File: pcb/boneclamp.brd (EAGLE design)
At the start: 160 x 100 mm, 39 parts, among them U1 AD7656YSTZ, U2 AD5754RBREZ, U3 SN74ABT541BDW, U4 ADP3303ARZ-5, U5 ADP3303ARZ-5

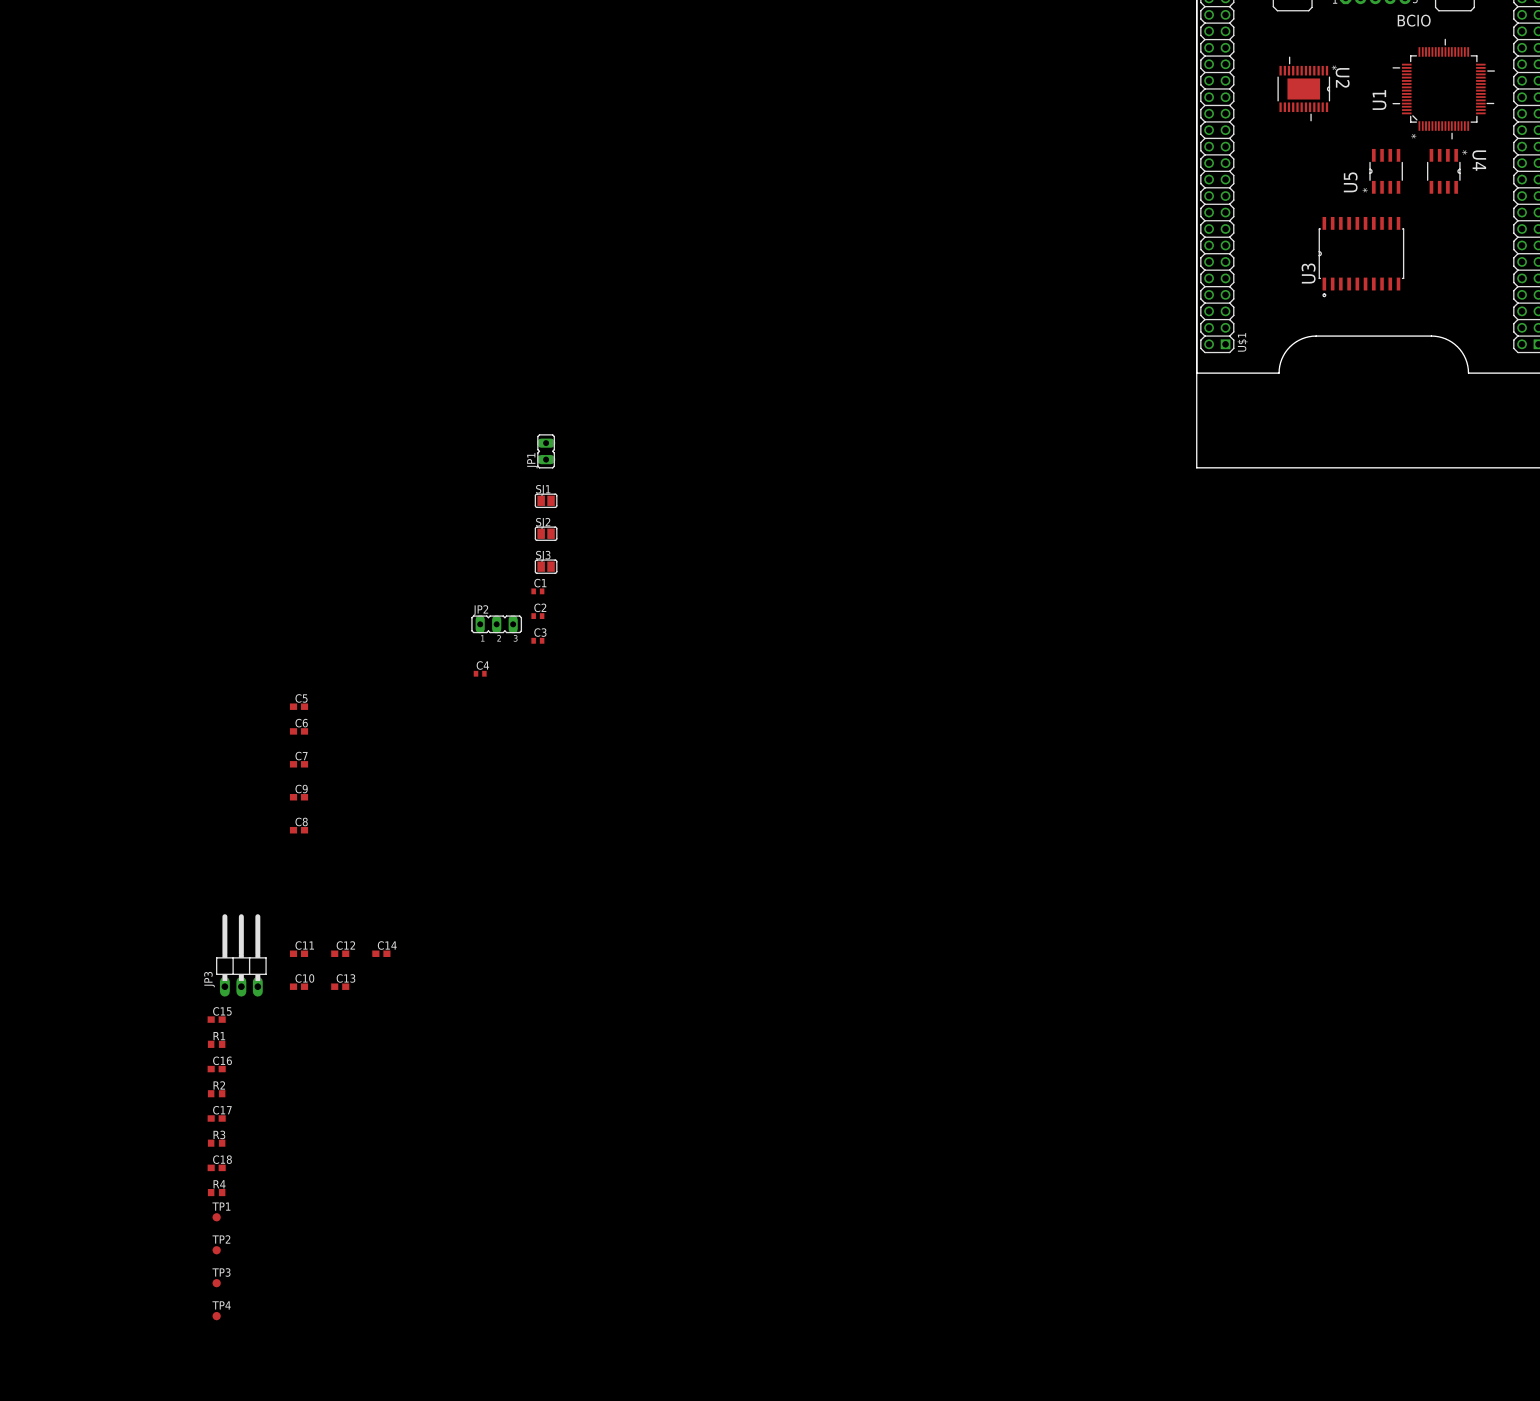
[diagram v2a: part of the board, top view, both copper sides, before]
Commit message: Found a good regulator for powering the BB using the +/- 6 to 12 volt rails required to use the boneclamp. Updated schematic and added data sheet to data-sheets folder
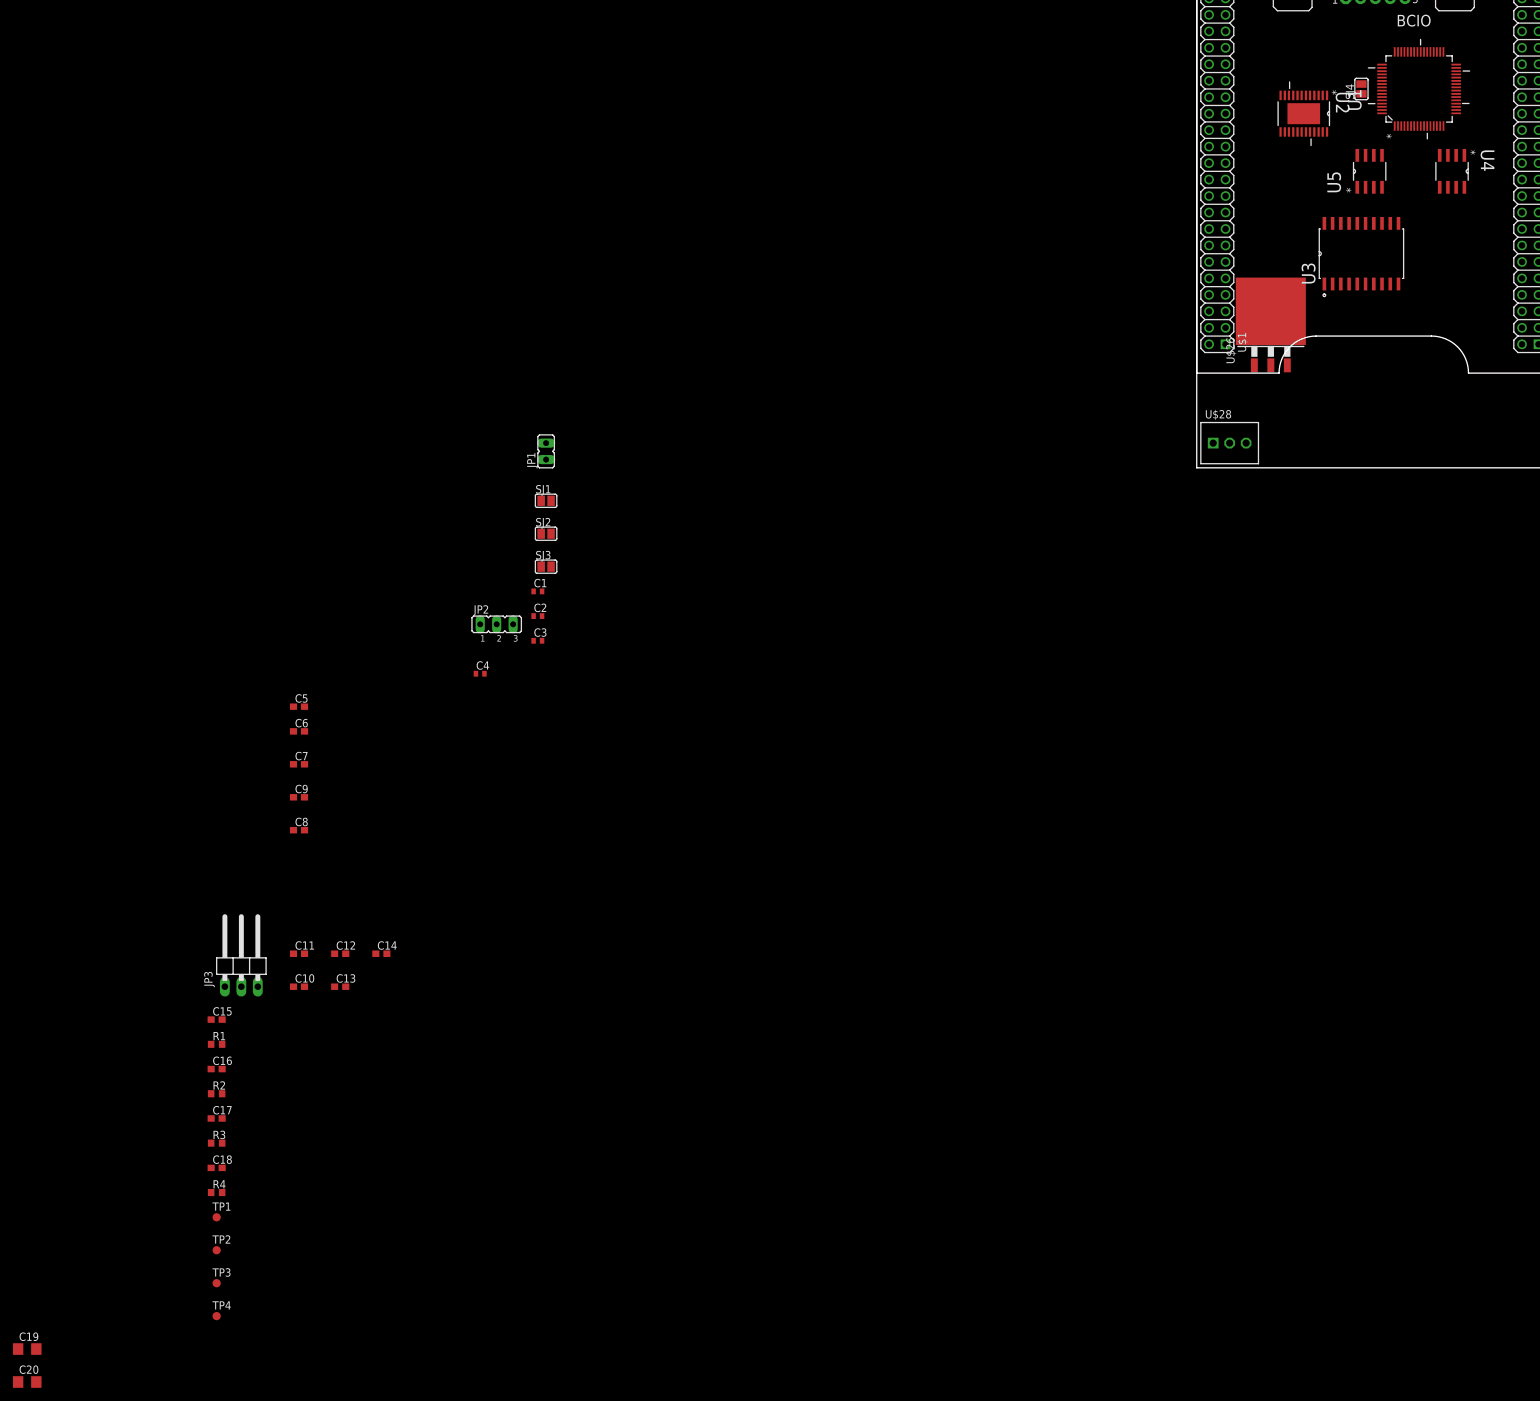
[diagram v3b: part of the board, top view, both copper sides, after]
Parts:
- added C19, C20: 10uF, rcl:C1206
- added SJ4: (no value), jumper:SJ
- added U$26: LM1085, boneclamp:TO263-3
- added U$28: SCREW3, boneclamp:SCREW3
- moved U1 3.81 mm to (34.3, 58.4)
- moved U2 3.81 mm to (16.5, 54.6)
- moved U5 2.54 mm to (26.7, 45.7)
- moved U4 1.27 mm to (39.4, 45.7)
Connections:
- new net +12V: C19.1, U$26.3
- new net -12V: U$28.P$3
- new net PGND: U$28.P$2
- net AGND: now also SJ4.1
- net DGND: now also C19.2, C20.2, SJ4.2, U$26.1
- net VDD_BB: now also C20.1, U$26.2, U$26.TAB

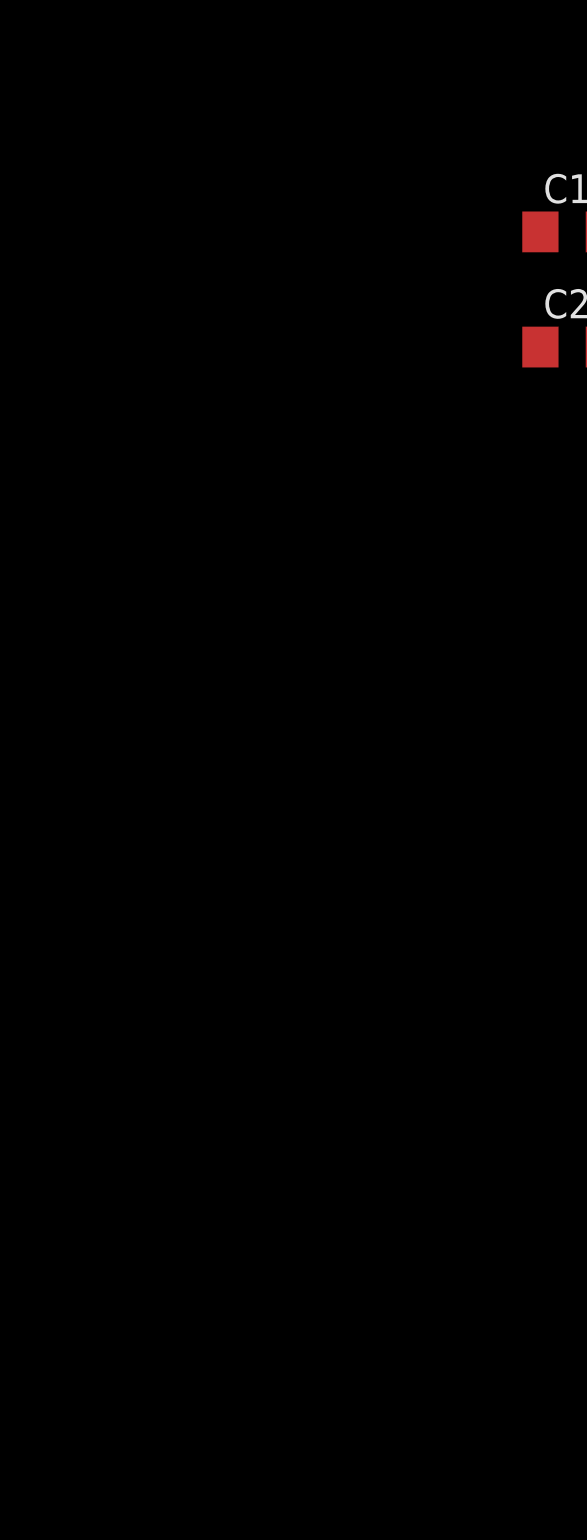
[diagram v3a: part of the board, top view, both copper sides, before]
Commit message: Added EEPROM to the I2C2bus to follow standard daughter board device ID requirements
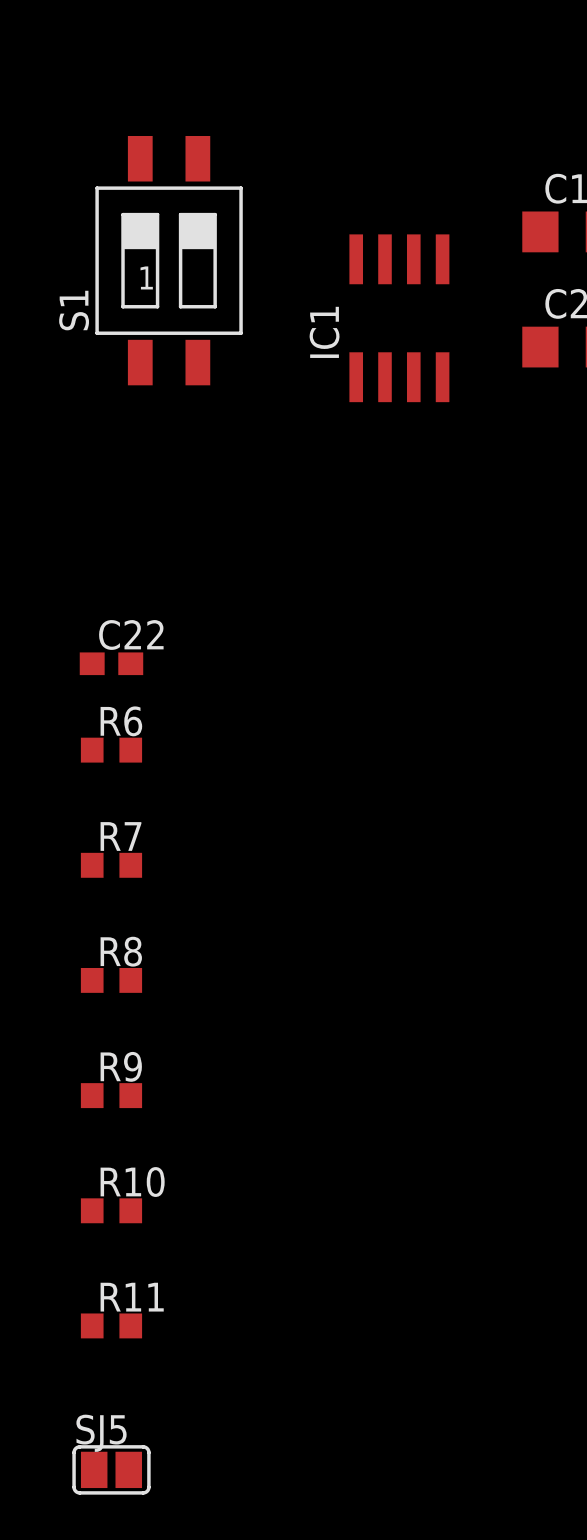
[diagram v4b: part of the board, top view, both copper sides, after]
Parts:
- added C22: 0.1uF, rcl:C0603
- added IC1: 24C, on-semiconductor-01:SO-08
- added R10, R6: 5.6k, rcl:R0603
- added R11: 10k, rcl:R0603
- added R7, R8, R9: 4.75k, rcl:R0603
- added S1: SWS002, smd-special:SMS-002
- added SJ5: (no value), jumper:SJ
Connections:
- removed net VDD_3V3EXP: U$1.50
- removed net VDD_5V: U$1.52
- new net I2C2_SCL: IC1.6, R10.1, U$1.65
- new net I2C2_SDA: IC1.5, R6.1, U$1.66
- new net N$14: IC1.1, R7.1, R8.1, S1.1
- new net N$18: IC1.2, S1.2
- new net N$19: IC1.3, R9.1
- new net N$21: IC1.7, SJ5.1
- new net N$22: R11.1, SJ5.2
- net BB_5V: now also U$1.54
- net DGND: now also C22.2, IC1.4, S1.3, S1.4
- net VDD_BB: now also U$1.52
- net VDRIVE: now also C22.1, IC1.8, R10.2, R11.2, R6.2, R7.2, R8.2, R9.2, U$1.50

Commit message: Added external 2.5 volt references for DAC and ADC. This circuit needs a buffer option which can be feed into the 3 position jumper.
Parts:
- added C23: 10uF, rcl:C1206
- added C24, C26, C27: 0.1uF, rcl:C0603
- added JP4, JP6: (no value), jumper:JP1
- added JP5: (no value), jumper:JP2
- added TP5: TPB1,27, testpad:B1,27
- added U6: ADR431BRZ, analog-devices-01:SOIC127P600X175-8N
- C10, C13, C5, C8: device rcl:C0603 -> rcl:C1206
- JP3: device pinhead:1X03/90 -> jumper:JP1
- moved C19 278.5 mm to (33.0, 43.2)
- moved C20 278.5 mm to (33.0, 38.1)
- moved IC1 278.5 mm to (25.4, 39.4)
- moved S1 278.5 mm to (15.2, 41.9)
- moved C22 278.5 mm to (12.7, 24.1)
- moved R10 278.5 mm to (12.7, 0.00)
- moved R11 278.5 mm to (12.7, -5.08)
- moved R6 278.5 mm to (12.7, 20.3)
- moved R7 278.5 mm to (12.7, 15.2)
- moved R8 278.5 mm to (12.7, 10.2)
- moved R9 278.5 mm to (12.7, 5.08)
- moved SJ5 278.5 mm to (12.7, -11.4)
- moved C15 226.3 mm to (8.89, 74.9)
- moved C18 226.3 mm to (8.89, 52.1)
- moved R1 226.3 mm to (8.89, 71.1)
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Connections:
- new net N$20: JP3.1, U1.51
- new net N$23: JP6.1
- new net N$24: JP4.1, U2.17
- new net N$25: C26.1, U6.1
- new net VREF_2.5V: JP3.2, JP4.2, JP5.2
- new net VREF_OUT: C27.1, JP5.3, JP6.2, TP5.TP, U6.6
- net AGND: now also C10.2, C23.2, C24.2, C26.2, U6.4; no longer C8.2
- net AVCC: now also C10.1; no longer C8.1
- net BB_5V: now also C8.1; no longer C10.1
- net DGND: now also C8.2; no longer C10.2
- net VDD: now also C23.1, C24.1, U6.2

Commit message: Added new data sheets. Started a second pcb layout for new DAC/ADC unipolar solutions.
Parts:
- added U$42: AD5686RARUZ, analog-devices-02:MO-153-AB
- added U7: AD7682BCPZ, analog-devices-02:QFN50P400X400X100-21N
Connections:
- new net VDD_2: U7.1
- new net VIO: U7.15
- net VDD: now also U$42.5, U7.20
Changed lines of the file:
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@@
 <element name="JP5" library="jumper" package="JP2" value="" x="-19.05" y="-1.27"/>
 <element name="JP6" library="jumper" package="JP1" value="" x="-26.67" y="-2.54"/>
+<element name="U$42" library="analog-devices-02" package="MO-153-AB" value="AD5686RARUZ" x="-68.58" y="-20.32"/>
+<element name="U7" library="analog-devices-02" package="QFN50P400X400X100-21N" value="AD7682BCPZ" x="-82.55" y="-20.32">
+<attribute name="PACKAGE" value="20-LFCSP" x="-82.55" y="-20.32" size="1.778" layer="27" display="off"/>
+<attribute name="OC_NEWARK" value="14N5814" x="-82.55" y="-20.32" size="1.778" layer="27" display="off"/>
+<attribute name="MPN" value="AD7682BCPZ" x="-82.55" y="-20.32" size="1.778" layer="27" display="off"/>
+<attribute name="SUPPLIER" value="Analog Devices" x="-82.55" y="-20.32" size="1.778" layer="27" display="off"/>
+<attribute name="OC_FARNELL" value="2067751" x="-82.55" y="-20.32" size="1.778" layer="27" display="off"/>
+</element>
 </elements>
 <signals>
@@
 <contactref element="C24" pad="1"/>
 <contactref element="C23" pad="1"/>
-<wire x1="-53.34" y1="46.57" x2="-12.83" y2="1.27" width="0" layer="19" extent="1-1"/>
-<wire x1="-49.4538" y1="48.895" x2="-53.34" y2="46.57" width="0" layer="19" extent="1-1"/>
-<wire x1="20.0914" y1="51.7906" x2="-49.4538" y2="48.895" width="0" layer="19" extent="1-1"/>
-<wire x1="99.695" y1="95.9612" x2="20.0914" y2="51.7906" width="0" layer="19" extent="1-1"/>
+<contactref element="U$42" pad="5"/>
+<contactref element="U7" pad="20"/>
+<wire x1="20.0914" y1="51.7906" x2="99.695" y2="95.9612" width="0" layer="19" extent="1-1"/>
+<wire x1="-12.83" y1="1.27" x2="20.0914" y2="51.7906" width="0" layer="19" extent="1-1"/>
+<wire x1="-49.4538" y1="48.895" x2="-12.83" y2="1.27" width="0" layer="19" extent="1-1"/>
+<wire x1="-53.34" y1="46.57" x2="-49.4538" y2="48.895" width="0" layer="19" extent="1-1"/>
+<wire x1="-71.3994" y1="-20.6502" x2="-12.83" y2="1.27" width="0" layer="19" extent="1-1"/>
+<wire x1="-83.5406" y1="-18.542" x2="-71.3994" y2="-20.6502" width="0" layer="19" extent="1-1"/>
 </signal>
 <signal name="DVCC">
@@
 <contactref element="JP6" pad="1"/>
 </signal>
+<signal name="VDD_2">
+<contactref element="U7" pad="1"/>
+</signal>
+<signal name="VIO">
+<contactref element="U7" pad="15"/>
+</signal>
 </signals>
